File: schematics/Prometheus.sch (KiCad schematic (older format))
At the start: 15 parts, among them J1 ATX Power Conn, SW2 Power Switch, U1 wdc65c816, U2 DS1501YN, X1 8MHz, X2 32kHz

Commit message: rearrange schematic page
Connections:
- net labels added: RTC_EN
- net labels removed: RTCEN
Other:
- moved on the sheet: BT1, D1, J1, R3, R?, SW2B, SW?A, U1, U2, X1, X2

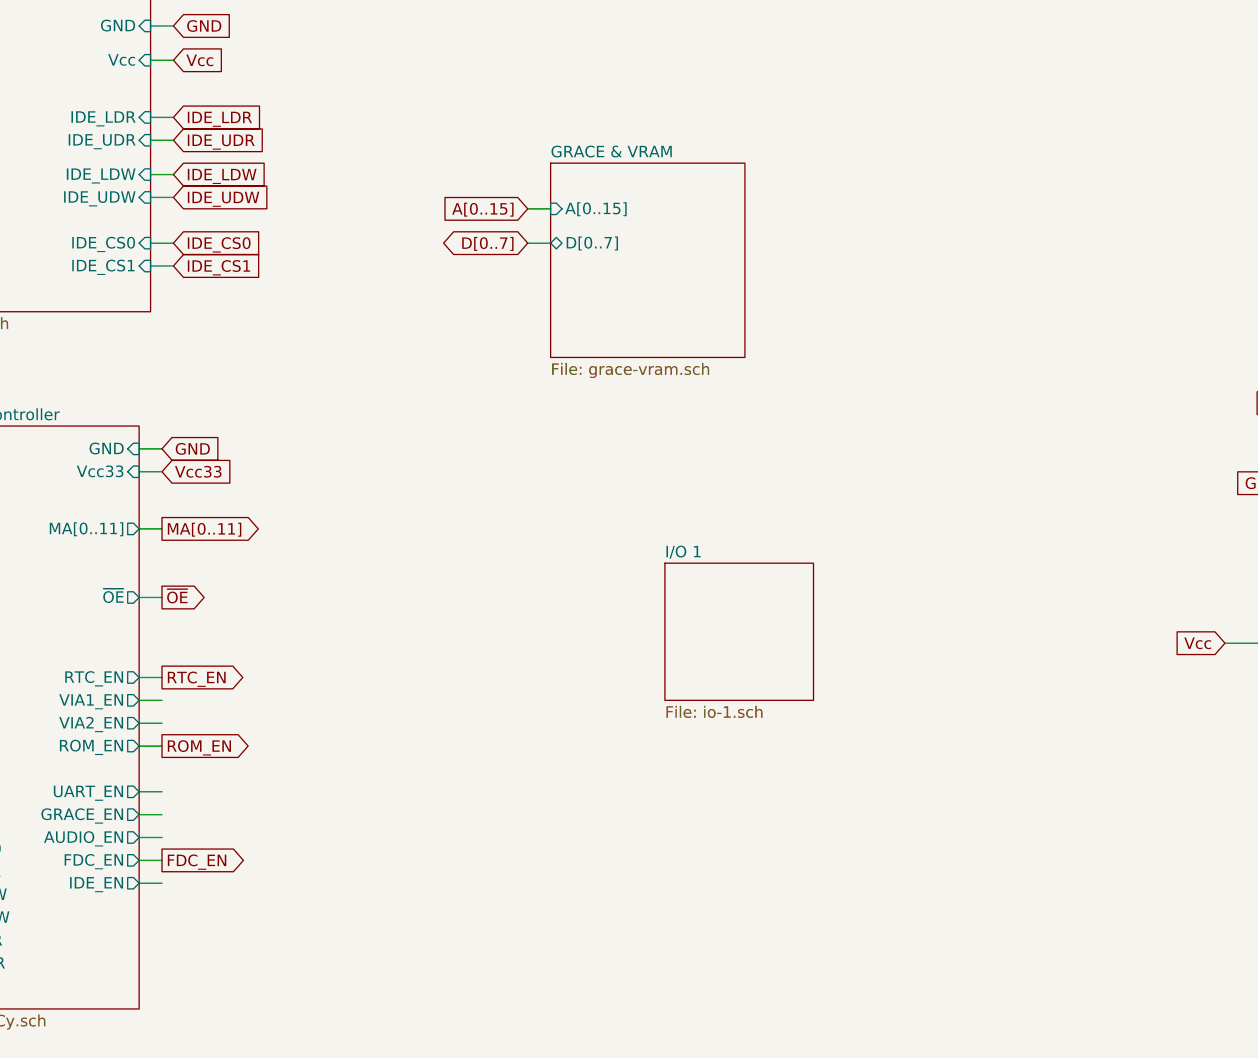
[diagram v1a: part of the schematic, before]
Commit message: Finish connecting hierarchial pins
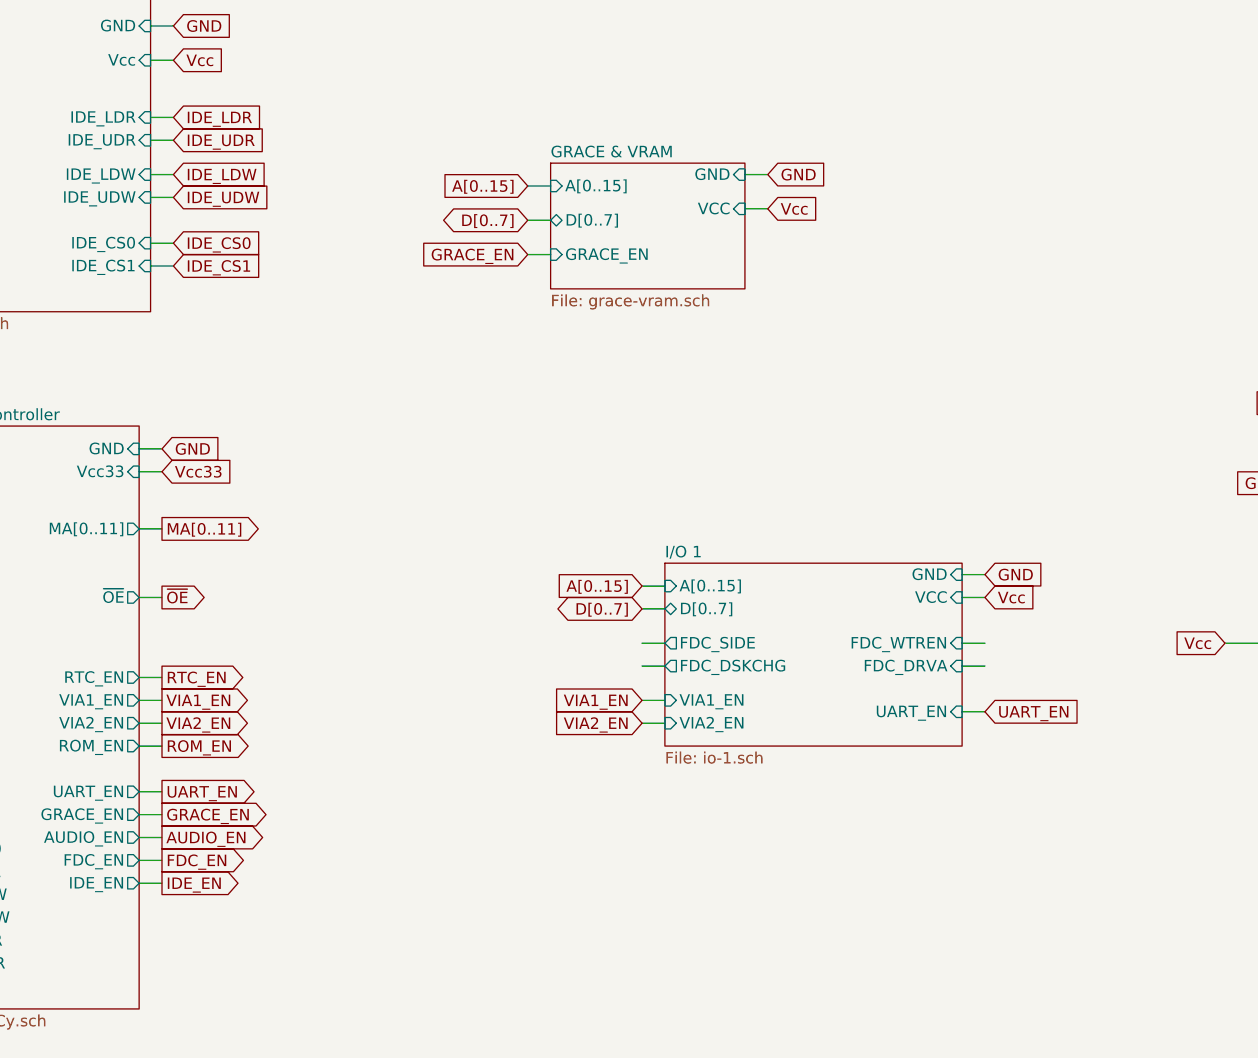
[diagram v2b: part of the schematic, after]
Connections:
- net labels added: AUDIO_EN, GRACE_EN, IDE_EN, UART_EN, VIA1_EN, VIA2_EN
- wire segments 183 -> 197
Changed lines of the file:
@@
 Wire Wire Line
 	8300 4550 8100 4550
-Text GLabel 3850 3700 0    50   Input ~ 0
+Text GLabel 3850 3600 0    50   Input ~ 0
 A[0..15]
 Wire Wire Line
-	3950 3700 3850 3700
-Text GLabel 3850 3850 0    50   BiDi ~ 0
+	3950 3600 3850 3600
+Text GLabel 3850 3750 0    50   BiDi ~ 0
 D[0..7]
 Wire Wire Line
-	3950 3850 3850 3850
+	3950 3750 3850 3750
 $Sheet
-S 3950 3500 850  850
+S 3950 3500 850  550
 U 5EF72E92
 F0 "GRACE & VRAM" 50
 F1 "grace-vram.sch" 50
-F2 "A[0..15]" I L 3950 3700 50
-F3 "D[0..7]" B L 3950 3850 50
-$EndSheet
-$Sheet
-S 4450 5250 650  600
-U 5F475375
-F0 "I/O 1" 50
-F1 "io-1.sch" 50
+F2 "A[0..15]" I L 3950 3600 50
+F3 "D[0..7]" B L 3950 3750 50
+F4 "GRACE_EN" I L 3950 3900 50
+F5 "VCC" I R 4800 3700 50
+F6 "GND" I R 4800 3550 50
 $EndSheet
 $Sheet
@@
 Text GLabel 2250 5750 2    50   Output ~ 0
 RTC_EN
+Wire Wire Line
+	3950 3900 3850 3900
+Wire Wire Line
+	4800 3550 4900 3550
+Wire Wire Line
+	4800 3700 4900 3700
+Text GLabel 4900 3550 2    50   Input ~ 0
+GND
+Text GLabel 4900 3700 2    50   Input ~ 0
+Vcc
+Text GLabel 3850 3900 0    50   Input ~ 0
+GRACE_EN
+$Sheet
+S 4450 5250 1300 800
+U 5F475375
+F0 "I/O 1" 50
+F1 "io-1.sch" 50
+F2 "VCC" I R 5750 5400 50
+F3 "GND" I R 5750 5300 50
+F4 "FDC_SIDE" O L 4450 5600 50
+F5 "FDC_WTREN" I R 5750 5600 50
+F6 "FDC_DSKCHG" O L 4450 5700 50
+F7 "FDC_DRVA" I R 5750 5700 50
+F8 "A[0..15]" I L 4450 5350 50
+F9 "D[0..7]" B L 4450 5450 50
+F10 "VIA1_EN" I L 4450 5850 50
+F11 "VIA2_EN" I L 4450 5950 50
+F12 "UART_EN" I R 5750 5900 50
+$EndSheet
+Wire Wire Line
+	4450 5350 4350 5350
+Wire Wire Line
+	4450 5450 4350 5450
+Wire Wire Line
+	4450 5600 4350 5600
+Wire Wire Line
+	4450 5700 4350 5700
+Wire Wire Line
+	4350 5850 4450 5850
+Wire Wire Line
+	4450 5950 4350 5950
+Wire Wire Line
+	5750 5300 5850 5300
+Wire Wire Line
+	5750 5400 5850 5400
+Wire Wire Line
+	5750 5600 5850 5600
+Wire Wire Line
+	5750 5700 5850 5700
+Wire Wire Line
+	5750 5900 5850 5900
 Wire Bus Line
 	5800 2150 5800 2500
@@
 Wire Bus Line
 	8500 1950 8500 3150
+Text GLabel 2250 5850 2    50   Output ~ 0
+VIA1_EN
+Text GLabel 2250 5950 2    50   Output ~ 0
+VIA2_EN
+Text GLabel 4350 5850 0    50   Input ~ 0
+VIA1_EN
+Text GLabel 4350 5950 0    50   Input ~ 0
+VIA2_EN
+Text GLabel 5850 5300 2    50   Input ~ 0
+GND
+Text GLabel 5850 5400 2    50   Input ~ 0
+Vcc
+Text GLabel 4350 5350 0    50   Input ~ 0
+A[0..15]
+Text GLabel 4350 5450 0    50   BiDi ~ 0
+D[0..7]
+Text GLabel 2250 6250 2    50   Output ~ 0
+UART_EN
+Text GLabel 5850 5900 2    50   Input ~ 0
+UART_EN
+Text GLabel 2250 6350 2    50   Output ~ 0
+GRACE_EN
+Text GLabel 2250 6450 2    50   Output ~ 0
+AUDIO_EN
+Text GLabel 2250 6650 2    50   Output ~ 0
+IDE_EN
 $EndSCHEMATC

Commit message: finish up hierarchial pins (as they stand now)
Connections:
- wire segments 197 -> 206
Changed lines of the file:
@@
 D7
 $Sheet
-S 3600 1850 700  550
+S 3600 1850 850  1350
 U 5F16299B
 F0 "Audio" 50
 F1 "audio.sch" 50
+F2 "AUDIO_EN" I R 4450 2550 50
+F3 "R~W" I L 3600 2400 50
+F4 "~IRQ" O L 3600 2250 50
+F5 "RESET" I L 3600 2550 50
+F6 "PHI2" I L 3600 2700 50
+F7 "RAS" I L 3600 2900 50
+F8 "CAS" I L 3600 3050 50
+F9 "VCC" I R 4450 2050 50
+F10 "GND" I R 4450 1950 50
 $EndSheet
 Text GLabel 10000 1650 2    50   Output ~ 0
@@
 Wire Wire Line
 	5750 5900 5850 5900
-Wire Bus Line
-	5800 2150 5800 2500
-Wire Bus Line
-	7050 2050 7050 2500
-Wire Bus Line
-	5650 1650 5650 2050
-Wire Bus Line
-	9950 2650 9950 3150
-Wire Bus Line
-	10100 1850 10100 2650
-Wire Bus Line
-	8500 1950 8500 3150
 Text GLabel 2250 5850 2    50   Output ~ 0
 VIA1_EN
@@
 Text GLabel 2250 6650 2    50   Output ~ 0
 IDE_EN
+Wire Wire Line
+	4450 1950 4550 1950
+Wire Wire Line
+	4450 2050 4550 2050
+Wire Wire Line
+	4450 2550 4550 2550
+Wire Wire Line
+	3600 2250 3500 2250
+Wire Wire Line
+	3600 2400 3500 2400
+Wire Wire Line
+	3600 2550 3500 2550
+Wire Wire Line
+	3600 2700 3500 2700
+Wire Wire Line
+	3600 2900 3500 2900
+Wire Wire Line
+	3600 3050 3500 3050
+Wire Bus Line
+	5800 2150 5800 2500
+Wire Bus Line
+	7050 2050 7050 2500
+Wire Bus Line
+	5650 1650 5650 2050
+Wire Bus Line
+	9950 2650 9950 3150
+Wire Bus Line
+	10100 1850 10100 2650
+Wire Bus Line
+	8500 1950 8500 3150
+Text GLabel 4550 1950 2    50   Input ~ 0
+GND
+Text GLabel 4550 2050 2    50   Input ~ 0
+Vcc
+Text GLabel 3500 2400 0    50   Input ~ 0
+RW
+Text GLabel 3500 2250 0    50   Output ~ 0
+IRQ
+Text GLabel 3500 2700 0    50   Input ~ 0
+PHI2
+Text GLabel 3500 2550 0    50   Input ~ 0
+RES
+Text GLabel 4550 2550 2    50   Input ~ 0
+AUDIO_EN
+Text GLabel 3500 3050 0    50   Input ~ 0
+CAS
+Text GLabel 3500 2900 0    50   Input ~ 0
+RAS
 $EndSCHEMATC

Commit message: additional fixups
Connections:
- net labels added: FDC_DRVA, FDC_DSKCHG, FDC_MTREN, FDC_SIDE
- wire segments 206 -> 210
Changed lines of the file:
@@
-$EndSheet
-$Sheet
-S 1150 2750 1050 1400
-U 5F47C633
-F0 "I/O 2" 50
-F1 "io-2.sch" 50
-F2 "D[0..7]" B L 1150 3050 50
-F3 "IRQ" O L 1150 3200 50
-F4 "FDC_EN" I L 1150 3450 50
-F5 "R~W" I L 1150 3600 50
-F6 "Vcc" I R 2200 3050 50
-F7 "GND" I R 2200 2900 50
-F8 "IOR" I L 1150 3750 50
-F9 "IOW" I L 1150 3900 50
-F10 "RESET" I L 1150 4050 50
-F11 "IDE_LDR" I R 2200 3300 50
-F12 "IDE_LDW" I R 2200 3550 50
-F13 "IDE_UDR" I R 2200 3400 50
-F14 "IDE_UDW" I R 2200 3650 50
-F15 "IRQ_HIGH" O L 1150 3300 50
-F16 "A[0..15]" I L 1150 2900 50
-F17 "IDE_CS0" I R 2200 3850 50
-F18 "IDE_CS1" I R 2200 3950 50
 $EndSheet
 $Sheet
@@
 	10150 6300 10650 6300
 Connection ~ 10150 6300
-Text GLabel 2300 2900 2    50   Input ~ 0
-GND
-Text GLabel 2300 3050 2    50   Input ~ 0
-Vcc
-Text GLabel 1050 2900 0    50   Input ~ 0
+Text GLabel 2300 2550 2    50   Input ~ 0
+GND
+Text GLabel 2300 2700 2    50   Input ~ 0
+Vcc
+Text GLabel 1050 2550 0    50   Input ~ 0
 A[0..15]
-Text GLabel 1050 3200 0    50   Output ~ 0
+Text GLabel 1050 2850 0    50   Output ~ 0
 IRQ
-Text GLabel 1050 3600 0    50   Input ~ 0
+Text GLabel 1050 3250 0    50   Input ~ 0
 RW
-Text GLabel 1050 4050 0    50   Input ~ 0
+Text GLabel 1050 3700 0    50   Input ~ 0
 RES
 Wire Wire Line
-	1050 4050 1150 4050
-Wire Wire Line
-	1050 3600 1150 3600
-Wire Wire Line
-	1050 3200 1150 3200
-Wire Wire Line
-	1050 2900 1150 2900
-Wire Wire Line
-	2200 2900 2300 2900
-Wire Wire Line
-	2200 3050 2300 3050
+	1050 3700 1150 3700
+Wire Wire Line
+	1050 3250 1150 3250
+Wire Wire Line
+	1050 2850 1150 2850
+Wire Wire Line
+	1050 2550 1150 2550
+Wire Wire Line
+	2200 2550 2300 2550
+Wire Wire Line
+	2200 2700 2300 2700
 $Sheet
 S 1250 1250 850  800
@@
 A[0..15]
 Wire Wire Line
-	1150 3050 1050 3050
-Text GLabel 1050 3050 0    50   BiDi ~ 0
+	1150 2700 1050 2700
+Text GLabel 1050 2700 0    50   BiDi ~ 0
 D[0..7]
 Text GLabel 1150 1500 0    50   BiDi ~ 0
@@
 PHI2
 Wire Wire Line
-	1150 3750 1050 3750
-Wire Wire Line
-	1150 3900 1050 3900
-Text GLabel 1050 3750 0    50   Input ~ 0
+	1150 3400 1050 3400
+Wire Wire Line
+	1150 3550 1050 3550
+Text GLabel 1050 3400 0    50   Input ~ 0
 IOR
-Text GLabel 1050 3900 0    50   Input ~ 0
+Text GLabel 1050 3550 0    50   Input ~ 0
 IOW
 Text GLabel 1100 6400 0    50   Output ~ 0
@@
 Text GLabel 2250 6550 2    50   Output ~ 0
 FDC_EN
-Text GLabel 1000 3450 0    50   Input ~ 0
+Text GLabel 1000 3100 0    50   Input ~ 0
 FDC_EN
 Wire Wire Line
-	1000 3450 1150 3450
-Wire Wire Line
-	1150 3300 1050 3300
+	1000 3100 1150 3100
+Wire Wire Line
+	1150 2950 1050 2950
+Wire Wire Line
+	2200 2950 2300 2950
+Wire Wire Line
+	2200 3050 2300 3050
+Wire Wire Line
+	2200 3200 2300 3200
 Wire Wire Line
 	2200 3300 2300 3300
-Wire Wire Line
-	2200 3400 2300 3400
-Wire Wire Line
-	2200 3550 2300 3550
-Wire Wire Line
-	2200 3650 2300 3650
+Text GLabel 2300 2950 2    50   Input ~ 0
+IDE_LDR
+Text GLabel 2300 3050 2    50   Input ~ 0
+IDE_UDR
+Text GLabel 2300 3200 2    50   Input ~ 0
+IDE_LDW
 Text GLabel 2300 3300 2    50   Input ~ 0
-IDE_LDR
-Text GLabel 2300 3400 2    50   Input ~ 0
-IDE_UDR
-Text GLabel 2300 3550 2    50   Input ~ 0
-IDE_LDW
-Text GLabel 2300 3650 2    50   Input ~ 0
 IDE_UDW
 Text GLabel 1100 6900 0    50   Output ~ 0
@@
 ROM_EN
 Wire Wire Line
-	2200 3850 2300 3850
-Wire Wire Line
-	2200 3950 2300 3950
+	2200 3500 2300 3500
+Wire Wire Line
+	2200 3600 2300 3600
 Text GLabel 1100 6500 0    50   Output ~ 0
 IDE_CS0
 Text GLabel 1100 6600 0    50   Output ~ 0
 IDE_CS1
-Text GLabel 2300 3850 2    50   Input ~ 0
+Text GLabel 2300 3500 2    50   Input ~ 0
 IDE_CS0
-Text GLabel 2300 3950 2    50   Input ~ 0
+Text GLabel 2300 3600 2    50   Input ~ 0
 IDE_CS1
 Text GLabel 2250 5750 2    50   Output ~ 0
@@
 Text GLabel 3850 3900 0    50   Input ~ 0
 GRACE_EN
-$Sheet
-S 4450 5250 1300 800
-U 5F475375
-F0 "I/O 1" 50
-F1 "io-1.sch" 50
-F2 "VCC" I R 5750 5400 50
-F3 "GND" I R 5750 5300 50
-F4 "FDC_SIDE" O L 4450 5600 50
-F5 "FDC_WTREN" I R 5750 5600 50
-F6 "FDC_DSKCHG" O L 4450 5700 50
-F7 "FDC_DRVA" I R 5750 5700 50
-F8 "A[0..15]" I L 4450 5350 50
-F9 "D[0..7]" B L 4450 5450 50
-F10 "VIA1_EN" I L 4450 5850 50
-F11 "VIA2_EN" I L 4450 5950 50
-F12 "UART_EN" I R 5750 5900 50
-$EndSheet
 Wire Wire Line
 	4450 5350 4350 5350
@@
 	4450 5450 4350 5450
 Wire Wire Line
-	4450 5600 4350 5600
-Wire Wire Line
-	4450 5700 4350 5700
-Wire Wire Line
 	4350 5850 4450 5850
 Wire Wire Line
@@
 Wire Wire Line
 	5750 5400 5850 5400
-Wire Wire Line
-	5750 5600 5850 5600
-Wire Wire Line
-	5750 5700 5850 5700
 Wire Wire Line
 	5750 5900 5850 5900
@@
 Wire Wire Line
 	3600 3050 3500 3050
-Wire Bus Line
-	5800 2150 5800 2500
-Wire Bus Line
-	7050 2050 7050 2500
-Wire Bus Line
-	5650 1650 5650 2050
-Wire Bus Line
-	9950 2650 9950 3150
-Wire Bus Line
-	10100 1850 10100 2650
-Wire Bus Line
-	8500 1950 8500 3150
 Text GLabel 4550 1950 2    50   Input ~ 0
 GND
@@
 Text GLabel 3500 2900 0    50   Input ~ 0
 RAS
+Wire Wire Line
+	4450 5700 4350 5700
+Wire Wire Line
+	4450 5600 4350 5600
+Wire Wire Line
+	5750 5700 5850 5700
+Wire Wire Line
+	5750 5600 5850 5600
+$Sheet
+S 4450 5250 1300 800
+U 5F475375
+F0 "I/O 1" 50
+F1 "io-1.sch" 50
+F2 "VCC" I R 5750 5400 50
+F3 "GND" I R 5750 5300 50
+F4 "FDC_SIDE" O L 4450 5600 50
+F5 "FDC_WTREN" I R 5750 5600 50
+F6 "FDC_DSKCHG" I L 4450 5700 50
+F7 "FDC_DRVA" O R 5750 5700 50
+F8 "A[0..15]" I L 4450 5350 50
+F9 "D[0..7]" B L 4450 5450 50
+F10 "VIA1_EN" I L 4450 5850 50
+F11 "VIA2_EN" I L 4450 5950 50
+F12 "UART_EN" I R 5750 5900 50
+$EndSheet
+$Sheet
+S 1150 2400 1050 1850
+U 5F47C633
+F0 "I/O 2" 50
+F1 "io-2.sch" 50
+F2 "D[0..7]" B L 1150 2700 50
+F3 "IRQ" O L 1150 2850 50
+F4 "FDC_EN" I L 1150 3100 50
+F5 "R~W" I L 1150 3250 50
+F6 "Vcc" I R 2200 2700 50
+F7 "GND" I R 2200 2550 50
+F8 "IOR" I L 1150 3400 50
+F9 "IOW" I L 1150 3550 50
+F10 "RESET" I L 1150 3700 50
+F11 "IDE_LDR" I R 2200 2950 50
+F12 "IDE_LDW" I R 2200 3200 50
+F13 "IDE_UDR" I R 2200 3050 50
+F14 "IDE_UDW" I R 2200 3300 50
+F15 "IRQ_HIGH" O L 1150 2950 50
+F16 "A[0..15]" I L 1150 2550 50
+F17 "IDE_CS0" I R 2200 3500 50
+F18 "IDE_CS1" I R 2200 3600 50
+F19 "FDC_SIDE" I L 1150 3900 50
+F20 "FDC_MTREN" O R 2200 3900 50
+F21 "FDC_DRVA" I L 1150 4050 50
+F22 "FDC_DSKCHG" O R 2200 4050 50
+$EndSheet
+Wire Wire Line
+	1150 3900 1050 3900
+Wire Wire Line
+	1150 4050 1050 4050
+Wire Wire Line
+	2200 3900 2300 3900
+Wire Wire Line
+	2200 4050 2300 4050
+Wire Bus Line
+	5800 2150 5800 2500
+Wire Bus Line
+	7050 2050 7050 2500
+Wire Bus Line
+	5650 1650 5650 2050
+Wire Bus Line
+	9950 2650 9950 3150
+Wire Bus Line
+	10100 1850 10100 2650
+Wire Bus Line
+	8500 1950 8500 3150
+Text GLabel 2300 3900 2    50   Output ~ 0
+FDC_MTREN
+Text GLabel 2300 4050 2    50   Output ~ 0
+FDC_DSKCHG
+Text GLabel 1050 3900 0    50   Input ~ 0
+FDC_SIDE
+Text GLabel 1050 4050 0    50   Input ~ 0
+FDC_DRVA
+Text GLabel 4350 5600 0    50   Output ~ 0
+FDC_SIDE
+Text GLabel 4350 5700 0    50   Input ~ 0
+FDC_DSKCHG
+Text GLabel 5850 5600 2    50   Input ~ 0
+FDC_MTREN
+Text GLabel 5850 5700 2    50   Input ~ 0
+FDC_DRVA
 $EndSCHEMATC
